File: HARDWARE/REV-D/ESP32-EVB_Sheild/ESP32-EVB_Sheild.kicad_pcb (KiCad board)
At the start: 2 copper layers, 6 parts

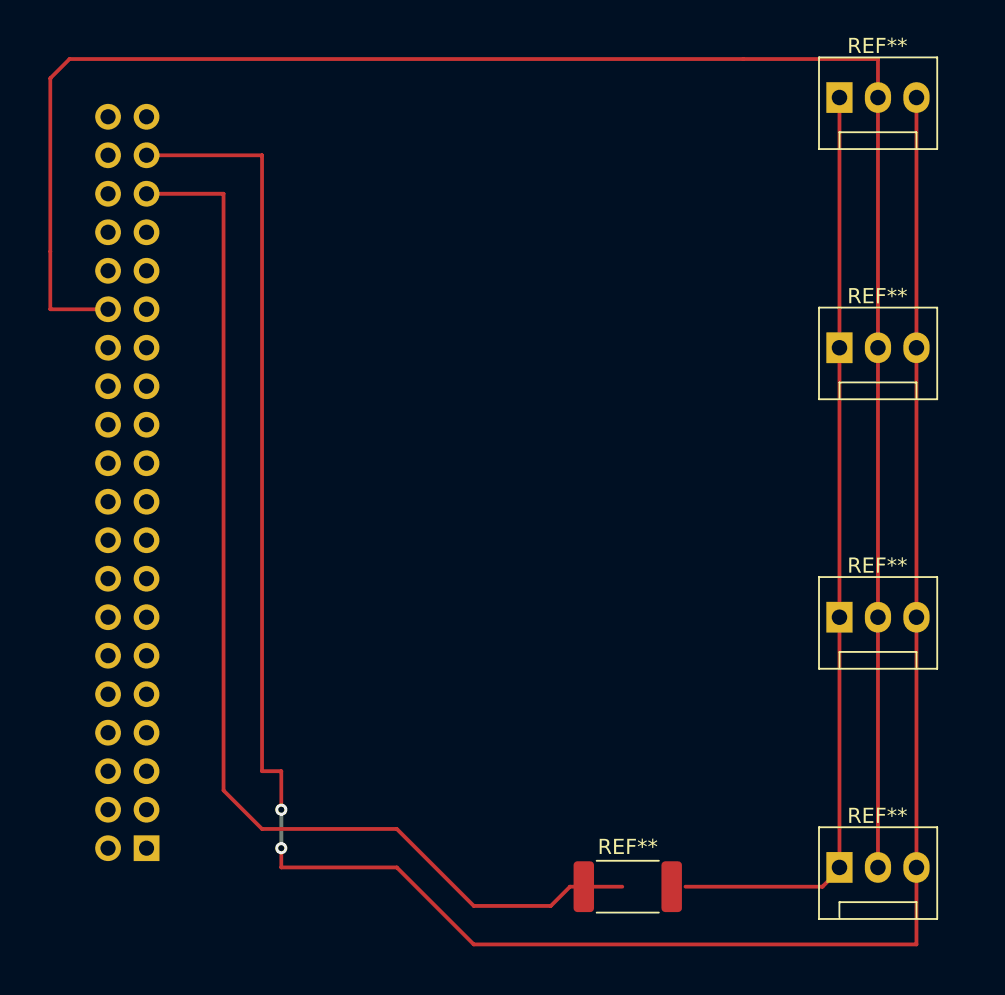
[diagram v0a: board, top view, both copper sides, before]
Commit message: added poly for board, and added schematic names
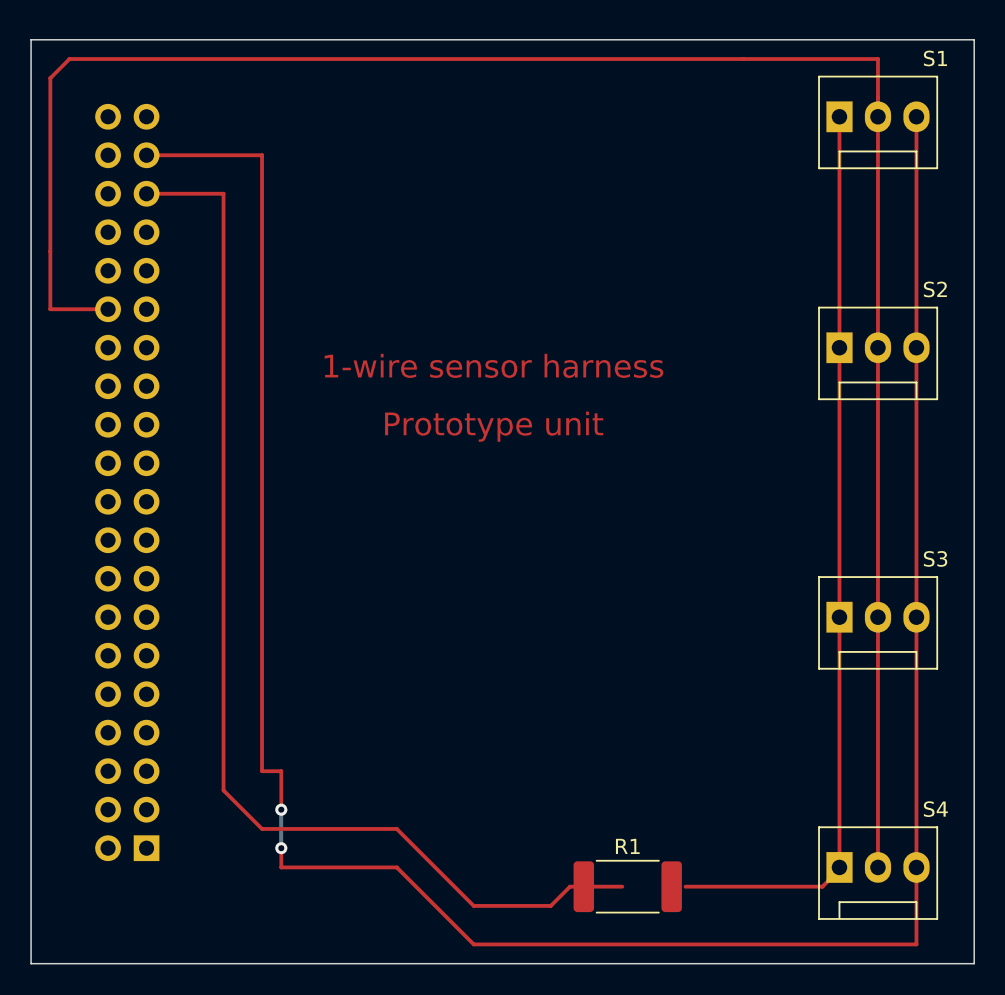
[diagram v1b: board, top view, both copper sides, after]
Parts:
- ESP32-DEV connector: renamed from REF**
- moved S1 1.27 mm to (130.8, 64.8)
- renumbered REF** to R1, REF** to S1, REF** to S2, REF** to S3, REF** to S4
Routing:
- net (no net): track 419.2 -> 416.6 mm
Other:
- board outline added: 62.2 x 61 mm
- board text added: "1-wire sensor harness"
- board text added: "Prototype unit"
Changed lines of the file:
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@@
   (general
     (thickness 1.6)
-    (drawings 0)
+    (drawings 6)
     (tracks 38)
     (zones 0)
@@
     (47 F.CrtYd user)
     (48 B.Fab user)
-    (49 F.Fab user)
+    (49 F.Fab user hide)
   )
   (setup
@@
     (tags resistor)
     (attr smd)
-    (fp_text reference REF** (at 0 -2.62) (layer F.SilkS)
+    (fp_text reference R1 (at 0 -2.62) (layer F.SilkS)
       (effects (font (size 1 1) (thickness 0.15)))
     )
@@
   )
   (module Connector:FanPinHeader_1x03_P2.54mm_Vertical (layer F.Cu)
-    (at 130.81 63.5)
+    (at 130.81 64.77)
     (descr "3-pin CPU fan Through hole pin header, see http://www.formfactors.org/developer%5Cspecs%5Crev1_2_public.pdf")
     (tags "pin header 3-pin CPU fan")
-    (fp_text reference REF** (at 2.5 -3.4) (layer F.SilkS)
+    (fp_text reference S1 (at 6.35 -3.81) (layer F.SilkS)
       (effects (font (size 1 1) (thickness 0.15)))
     )
@@
     (descr "3-pin CPU fan Through hole pin header, see http://www.formfactors.org/developer%5Cspecs%5Crev1_2_public.pdf")
     (tags "pin header 3-pin CPU fan")
-    (fp_text reference REF** (at 2.5 -3.4) (layer F.SilkS)
+    (fp_text reference S2 (at 6.35 -3.81) (layer F.SilkS)
       (effects (font (size 1 1) (thickness 0.15)))
     )
@@
     (descr "3-pin CPU fan Through hole pin header, see http://www.formfactors.org/developer%5Cspecs%5Crev1_2_public.pdf")
     (tags "pin header 3-pin CPU fan")
-    (fp_text reference REF** (at 2.5 -3.4) (layer F.SilkS)
+    (fp_text reference S3 (at 6.35 -3.81) (layer F.SilkS)
       (effects (font (size 1 1) (thickness 0.15)))
     )
@@
     (descr "3-pin CPU fan Through hole pin header, see http://www.formfactors.org/developer%5Cspecs%5Crev1_2_public.pdf")
     (tags "pin header 3-pin CPU fan")
-    (fp_text reference REF** (at 2.5 -3.4) (layer F.SilkS)
+    (fp_text reference S4 (at 6.35 -3.81) (layer F.SilkS)
       (effects (font (size 1 1) (thickness 0.15)))
     )
@@
     (descr "Through hole straight socket strip, 2x20, 2.54mm pitch, double cols (from Kicad 4.0.7), script generated")
     (tags "Through hole socket strip THT 2x20 2.54mm double row")
-    (fp_text reference REF** (at -1.27 2.77) (layer B.SilkS)
+    (fp_text reference "ESP32-DEV connector" (at 2.54 2.77) (layer B.SilkS)
       (effects (font (size 1 1) (thickness 0.15)) (justify mirror))
     )
-    (fp_text value PinSocket_2x20_P2.54mm_Vertical (at -1.27 -51.03) (layer B.Fab)
+    (fp_text value PinSocket_2x20_P2.54mm_Vertical (at -1.27 -50.8) (layer B.Fab)
       (effects (font (size 1 1) (thickness 0.15)) (justify mirror))
     )
@@
     )
   )
+  (gr_text "Prototype unit\n" (at 107.95 85.09) (layer F.Cu)
+    (effects (font (size 1.5 1.5) (thickness 0.3)))
+  )
+  (gr_text "1-wire sensor harness" (at 107.95 81.28) (layer F.Cu)
+    (effects (font (size 1.5 1.5) (thickness 0.3)))
+  )
+  (gr_line (start 139.7 59.69) (end 77.47 59.69) (layer Edge.Cuts) (width 0.1))
+  (gr_line (start 139.7 120.65) (end 139.7 59.69) (layer Edge.Cuts) (width 0.1))
+  (gr_line (start 77.47 120.65) (end 139.7 120.65) (layer Edge.Cuts) (width 0.1))
+  (gr_line (start 77.47 59.69) (end 77.47 120.65) (layer Edge.Cuts) (width 0.1))
   (segment (start 106.68 116.84) (end 111.76 116.84) (width 0.25) (layer F.Cu) (net 0))
   (segment (start 130.81 114.3) (end 130.81 97.79) (width 0.25) (layer F.Cu) (net 0))
@@
   (segment (start 113.03 115.57) (end 111.76 116.84) (width 0.25) (layer F.Cu) (net 0))
   (segment (start 116.48 115.57) (end 113.03 115.57) (width 0.25) (layer F.Cu) (net 0))
-  (segment (start 130.81 80.01) (end 130.81 63.5) (width 0.25) (layer F.Cu) (net 0))
   (segment (start 129.69 115.57) (end 130.81 114.45) (width 0.25) (layer F.Cu) (net 0))
   (segment (start 120.65 115.57) (end 129.69 115.57) (width 0.25) (layer F.Cu) (net 0))
@@
   (segment (start 135.89 114.3) (end 135.89 97.79) (width 0.25) (layer F.Cu) (net 0))
   (segment (start 135.89 97.79) (end 135.89 80.01) (width 0.25) (layer F.Cu) (net 0))
-  (segment (start 135.89 80.01) (end 135.89 63.5) (width 0.25) (layer F.Cu) (net 0))
   (segment (start 124.46 60.96) (end 133.35 60.96) (width 0.25) (layer F.Cu) (net 0))
   (segment (start 133.35 60.96) (end 133.35 63.5) (width 0.25) (layer F.Cu) (net 0))
@@
   (segment (start 93.98 114.3) (end 101.6 114.3) (width 0.25) (layer F.Cu) (net 0))
   (segment (start 93.98 110.49) (end 93.98 113.03) (width 0.25) (layer B.Cu) (net 0))
+  (segment (start 130.81 80.01) (end 130.81 64.77) (width 0.25) (layer F.Cu) (net 0))
+  (segment (start 135.89 64.77) (end 135.89 80.01) (width 0.25) (layer F.Cu) (net 0))
 )

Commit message: smaller clearance on edge - need to adjust for case
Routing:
- net (no net): track 416.6 -> 412.5 mm
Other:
- board size 62.2 x 61 mm -> 59.7 x 61 mm
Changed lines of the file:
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@@
     (thickness 1.6)
     (drawings 6)
-    (tracks 38)
+    (tracks 42)
     (zones 0)
     (modules 6)
@@
     (descr "Through hole straight socket strip, 2x20, 2.54mm pitch, double cols (from Kicad 4.0.7), script generated")
     (tags "Through hole socket strip THT 2x20 2.54mm double row")
-    (fp_text reference "ESP32-DEV connector" (at 2.54 2.77) (layer B.SilkS)
+    (fp_text reference "ESP32-DEV connector" (at 5.08 3.81) (layer B.SilkS)
       (effects (font (size 1 1) (thickness 0.15)) (justify mirror))
     )
@@
     (effects (font (size 1.5 1.5) (thickness 0.3)))
   )
-  (gr_line (start 139.7 59.69) (end 77.47 59.69) (layer Edge.Cuts) (width 0.1))
+  (gr_line (start 139.7 59.69) (end 80.01 59.69) (layer Edge.Cuts) (width 0.1))
   (gr_line (start 139.7 120.65) (end 139.7 59.69) (layer Edge.Cuts) (width 0.1))
-  (gr_line (start 77.47 120.65) (end 139.7 120.65) (layer Edge.Cuts) (width 0.1))
-  (gr_line (start 77.47 59.69) (end 77.47 120.65) (layer Edge.Cuts) (width 0.1))
+  (gr_line (start 80.01 120.65) (end 139.7 120.65) (layer Edge.Cuts) (width 0.1))
+  (gr_line (start 80.01 59.69) (end 80.01 120.65) (layer Edge.Cuts) (width 0.1))
   (segment (start 106.68 116.84) (end 111.76 116.84) (width 0.25) (layer F.Cu) (net 0))
-  (segment (start 130.81 114.3) (end 130.81 97.79) (width 0.25) (layer F.Cu) (net 0))
   (segment (start 130.81 97.79) (end 130.81 80.01) (width 0.25) (layer F.Cu) (net 0))
   (segment (start 113.03 115.57) (end 111.76 116.84) (width 0.25) (layer F.Cu) (net 0))
-  (segment (start 116.48 115.57) (end 113.03 115.57) (width 0.25) (layer F.Cu) (net 0))
   (segment (start 129.69 115.57) (end 130.81 114.45) (width 0.25) (layer F.Cu) (net 0))
-  (segment (start 120.65 115.57) (end 129.69 115.57) (width 0.25) (layer F.Cu) (net 0))
   (segment (start 92.71 111.76) (end 101.6 111.76) (width 0.25) (layer F.Cu) (net 0))
   (segment (start 101.6 111.76) (end 106.68 116.84) (width 0.25) (layer F.Cu) (net 0))
@@
   (segment (start 135.89 114.3) (end 135.89 97.79) (width 0.25) (layer F.Cu) (net 0))
   (segment (start 135.89 97.79) (end 135.89 80.01) (width 0.25) (layer F.Cu) (net 0))
-  (segment (start 124.46 60.96) (end 133.35 60.96) (width 0.25) (layer F.Cu) (net 0))
-  (segment (start 133.35 60.96) (end 133.35 63.5) (width 0.25) (layer F.Cu) (net 0))
-  (segment (start 133.35 63.5) (end 133.35 80.01) (width 0.25) (layer F.Cu) (net 0))
   (segment (start 133.35 80.01) (end 133.35 97.79) (width 0.25) (layer F.Cu) (net 0))
   (segment (start 133.35 97.79) (end 133.35 114.3) (width 0.25) (layer F.Cu) (net 0))
-  (segment (start 124.46 60.96) (end 80.01 60.96) (width 0.25) (layer F.Cu) (net 0))
-  (segment (start 80.01 60.96) (end 78.74 62.23) (width 0.25) (layer F.Cu) (net 0))
-  (segment (start 78.74 62.23) (end 78.74 73.66) (width 0.25) (layer F.Cu) (net 0))
-  (segment (start 78.74 73.66) (end 78.74 77.47) (width 0.25) (layer F.Cu) (net 0))
-  (segment (start 78.74 77.47) (end 82.55 77.47) (width 0.25) (layer F.Cu) (net 0))
   (segment (start 85.09 69.85) (end 90.17 69.85) (width 0.25) (layer F.Cu) (net 0))
   (segment (start 90.17 69.85) (end 90.17 109.22) (width 0.25) (layer F.Cu) (net 0))
@@
   (segment (start 130.81 80.01) (end 130.81 64.77) (width 0.25) (layer F.Cu) (net 0))
   (segment (start 135.89 64.77) (end 135.89 80.01) (width 0.25) (layer F.Cu) (net 0))
+  (segment (start 133.35 63.5) (end 133.35 80.01) (width 0.25) (layer F.Cu) (net 0))
+  (segment (start 133.35 60.96) (end 133.35 63.5) (width 0.25) (layer F.Cu) (net 0))
+  (segment (start 81.28 77.47) (end 81.28 76.2) (width 0.25) (layer F.Cu) (net 0))
+  (segment (start 82.55 77.47) (end 81.28 77.47) (width 0.25) (layer F.Cu) (net 0))
+  (segment (start 81.28 76.2) (end 80.38501 75.30501) (width 0.25) (layer F.Cu) (net 0))
+  (segment (start 80.38501 75.30501) (end 80.38501 63.12499) (width 0.25) (layer F.Cu) (net 0))
+  (segment (start 80.38501 63.12499) (end 82.55 60.96) (width 0.25) (layer F.Cu) (net 0))
+  (segment (start 82.55 60.96) (end 133.35 60.96) (width 0.25) (layer F.Cu) (net 0))
+  (segment (start 113.03 115.57) (end 113.94 115.57) (width 0.25) (layer F.Cu) (net 0))
+  (segment (start 120.65 115.57) (end 119.74 115.57) (width 0.25) (layer F.Cu) (net 0))
+  (segment (start 129.54 115.57) (end 130.81 114.3) (width 0.25) (layer F.Cu) (net 0))
+  (segment (start 129.54 115.57) (end 129.69 115.57) (width 0.25) (layer F.Cu) (net 0))
+  (segment (start 120.65 115.57) (end 129.54 115.57) (width 0.25) (layer F.Cu) (net 0))
+  (segment (start 130.81 113.03) (end 130.81 114.3) (width 0.25) (layer F.Cu) (net 0))
+  (segment (start 130.81 113.03) (end 130.81 97.79) (width 0.25) (layer F.Cu) (net 0))
 )

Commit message: Added 1 wire sensor interface with proper wiring, labels and shortened the pcb width.
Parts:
- R1: value R_2512_6332Metric -> R_0805_2012Metric; footprint Resistor_SMD:R_2512_6332Metric -> Resistor_SMD:R_0805_2012Metric
- moved R1 56.8 mm to (91.4, 64.8), turned to 90 degrees
- moved S1 25.4 mm to (105.4, 66.0)
- moved S2 25.4 mm to (105.4, 81.3)
- moved S3 25.4 mm to (105.4, 99.1)
- moved S4 25.4 mm to (105.4, 115.6)
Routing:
- net (no net): track 412.5 -> 345.7 mm
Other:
- board size 59.7 x 61 mm -> 33 x 61 mm
- board text added: "3v3"
- board text added: "GND"

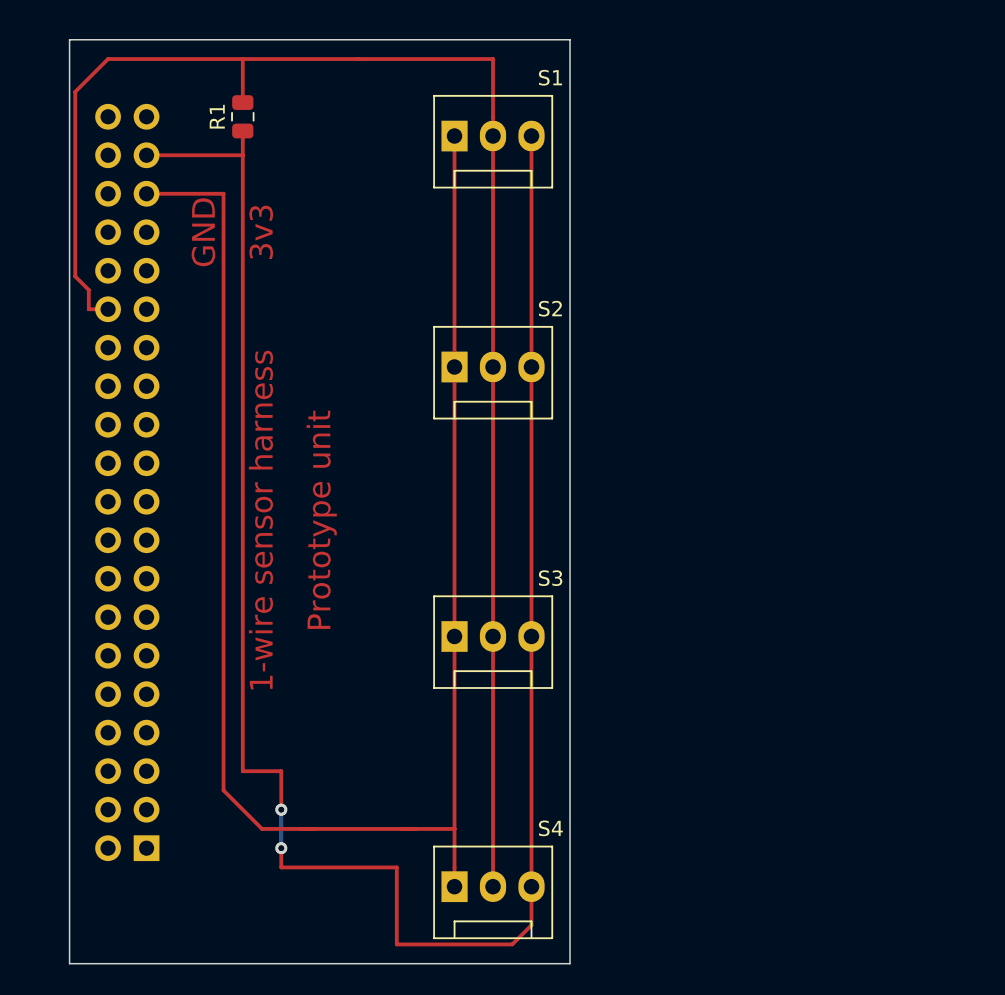
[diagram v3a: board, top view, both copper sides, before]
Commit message: tweaked board size to waste less pcb, need to measure relay clearance
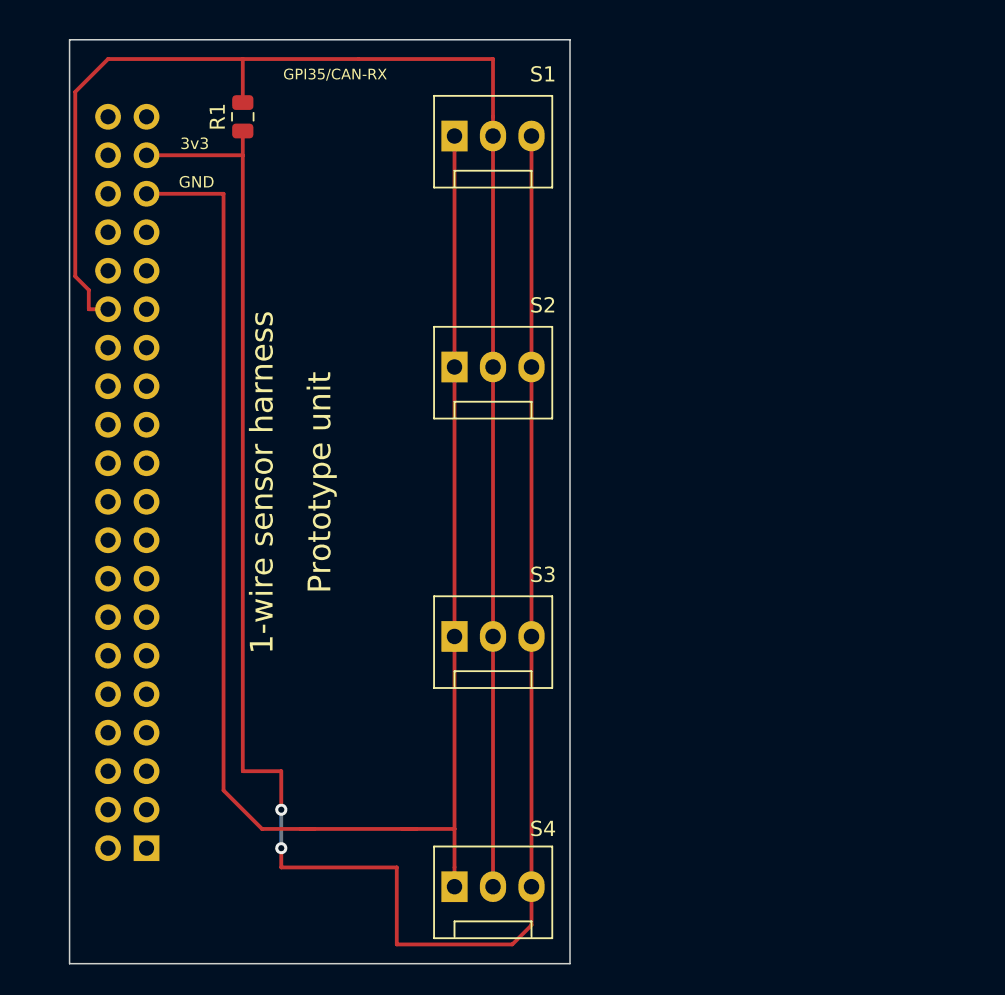
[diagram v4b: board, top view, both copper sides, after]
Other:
- board text added: "GPI35/CAN-RX"
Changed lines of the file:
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@@
   (general
     (thickness 1.6)
-    (drawings 8)
+    (drawings 9)
     (tracks 41)
     (zones 0)
@@
     (46 B.CrtYd user)
     (47 F.CrtYd user)
-    (48 B.Fab user)
+    (48 B.Fab user hide)
     (49 F.Fab user hide)
   )
@@
     (descr "3-pin CPU fan Through hole pin header, see http://www.formfactors.org/developer%5Cspecs%5Crev1_2_public.pdf")
     (tags "pin header 3-pin CPU fan")
-    (fp_text reference S1 (at 6.35 -3.81) (layer F.SilkS)
+    (fp_text reference S1 (at 5.842 -4.064) (layer F.SilkS)
       (effects (font (size 1 1) (thickness 0.15)))
     )
@@
     (descr "3-pin CPU fan Through hole pin header, see http://www.formfactors.org/developer%5Cspecs%5Crev1_2_public.pdf")
     (tags "pin header 3-pin CPU fan")
-    (fp_text reference S2 (at 6.35 -3.81) (layer F.SilkS)
+    (fp_text reference S2 (at 5.842 -4.064) (layer F.SilkS)
       (effects (font (size 1 1) (thickness 0.15)))
     )
@@
     (descr "3-pin CPU fan Through hole pin header, see http://www.formfactors.org/developer%5Cspecs%5Crev1_2_public.pdf")
     (tags "pin header 3-pin CPU fan")
-    (fp_text reference S3 (at 6.35 -3.81) (layer F.SilkS)
+    (fp_text reference S3 (at 5.842 -4.064) (layer F.SilkS)
       (effects (font (size 1 1) (thickness 0.15)))
     )
@@
     (descr "3-pin CPU fan Through hole pin header, see http://www.formfactors.org/developer%5Cspecs%5Crev1_2_public.pdf")
     (tags "pin header 3-pin CPU fan")
-    (fp_text reference S4 (at 6.35 -3.81) (layer F.SilkS)
+    (fp_text reference S4 (at 5.842 -3.81) (layer F.SilkS)
       (effects (font (size 1 1) (thickness 0.15)))
     )
@@
     )
   )
-  (gr_text GND (at 88.9 72.39 90) (layer F.Cu)
+  (gr_text GPI35/CAN-RX (at 97.536 61.976) (layer F.SilkS)
+    (effects (font (size 0.7 0.7) (thickness 0.175)))
+  )
+  (gr_text GND (at 88.392 69.088) (layer F.SilkS)
+    (effects (font (size 0.75 0.75) (thickness 0.1875)))
+  )
+  (gr_text 3v3 (at 88.265 66.548) (layer F.SilkS)
+    (effects (font (size 0.75 0.75) (thickness 0.1875)))
+  )
+  (gr_text "Prototype unit\n" (at 96.52 88.9 90) (layer F.SilkS)
     (effects (font (size 1.5 1.5) (thickness 0.3)))
   )
-  (gr_text 3v3 (at 92.71 72.39 90) (layer F.Cu)
+  (gr_text "1-wire sensor harness" (at 92.71 88.9 90) (layer F.SilkS)
     (effects (font (size 1.5 1.5) (thickness 0.3)))
   )
-  (gr_text "Prototype unit\n" (at 96.52 91.44 90) (layer F.Cu)
-    (effects (font (size 1.5 1.5) (thickness 0.3)))
-  )
-  (gr_text "1-wire sensor harness" (at 92.71 91.44 90) (layer F.Cu)
-    (effects (font (size 1.5 1.5) (thickness 0.3)))
-  )
